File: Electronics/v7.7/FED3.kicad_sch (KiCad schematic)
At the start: 41 parts, among them IC2 TB6612FNG, J2 Conn_01x02_Odd_Even, J3 USB4105-GF-A, SW1 Sw, U2 MIC5504-3.3, U3 MCP73834-xxxx, X3 B2B-PH-K-S

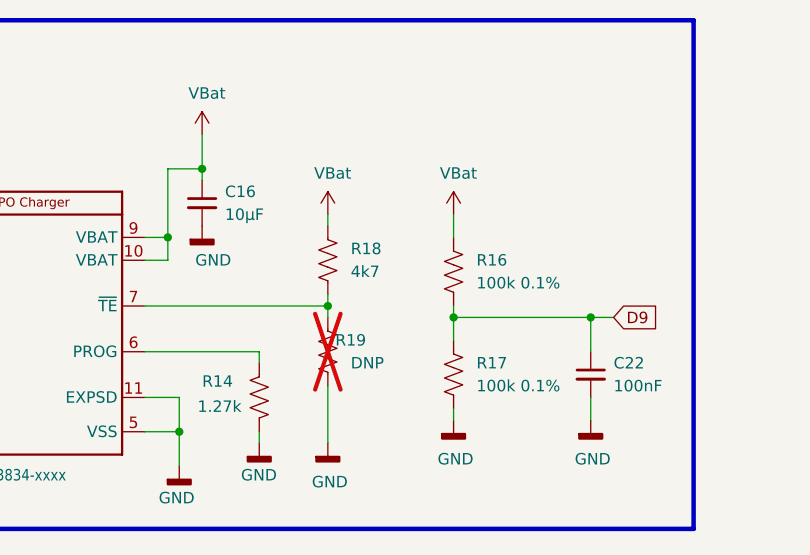
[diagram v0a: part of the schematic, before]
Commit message: Change R18 from 4.7k to 100k and update BOM
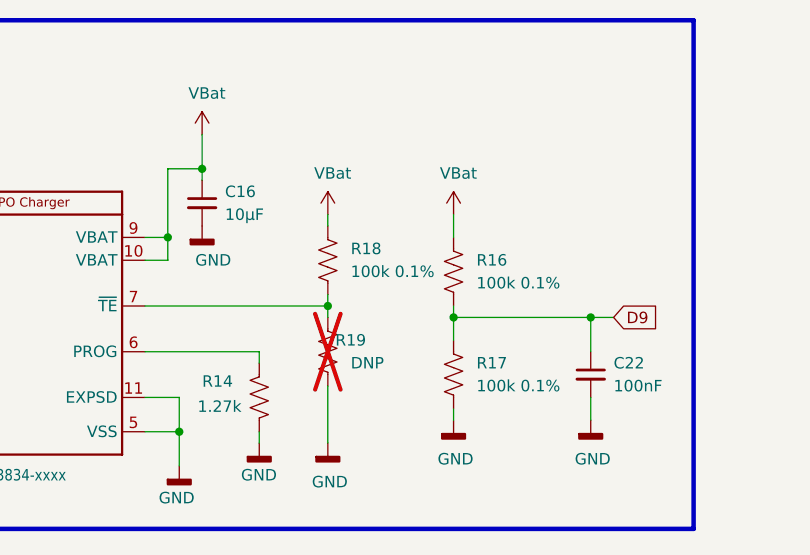
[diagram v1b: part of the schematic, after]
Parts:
- R18: value 4k7 -> 100k 0.1%; MPN ERJ-2RKF4701X -> RG1005P-104-B-T5; OEPSPN OEPS020010 -> OEPS020175
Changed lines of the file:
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@@
 			)
 		)
-		(property "Value" "4k7"
+		(property "Value" "100k 0.1%"
 			(at 241.3 41.9099 0)
 			(effects
@@
 			)
 		)
-		(property "Description" "SMD 0402 4.7k 1% 0.100W"
+		(property "Description" "SMD 0402 100kΩ ±0.1% 0.063W"
 			(at 238.76 40.64 0)
 			(effects
@@
 			)
 		)
-		(property "OEPSPN" "OEPS020010"
+		(property "OEPSPN" "OEPS020175"
 			(at 238.76 40.64 0)
 			(effects
@@
 			)
 		)
-		(property "MPN" "ERJ-2RKF4701X"
+		(property "MPN" "RG1005P-104-B-T5"
 			(at 238.76 40.64 0)
 			(effects
